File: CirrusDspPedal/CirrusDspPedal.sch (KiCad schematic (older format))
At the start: 0 parts

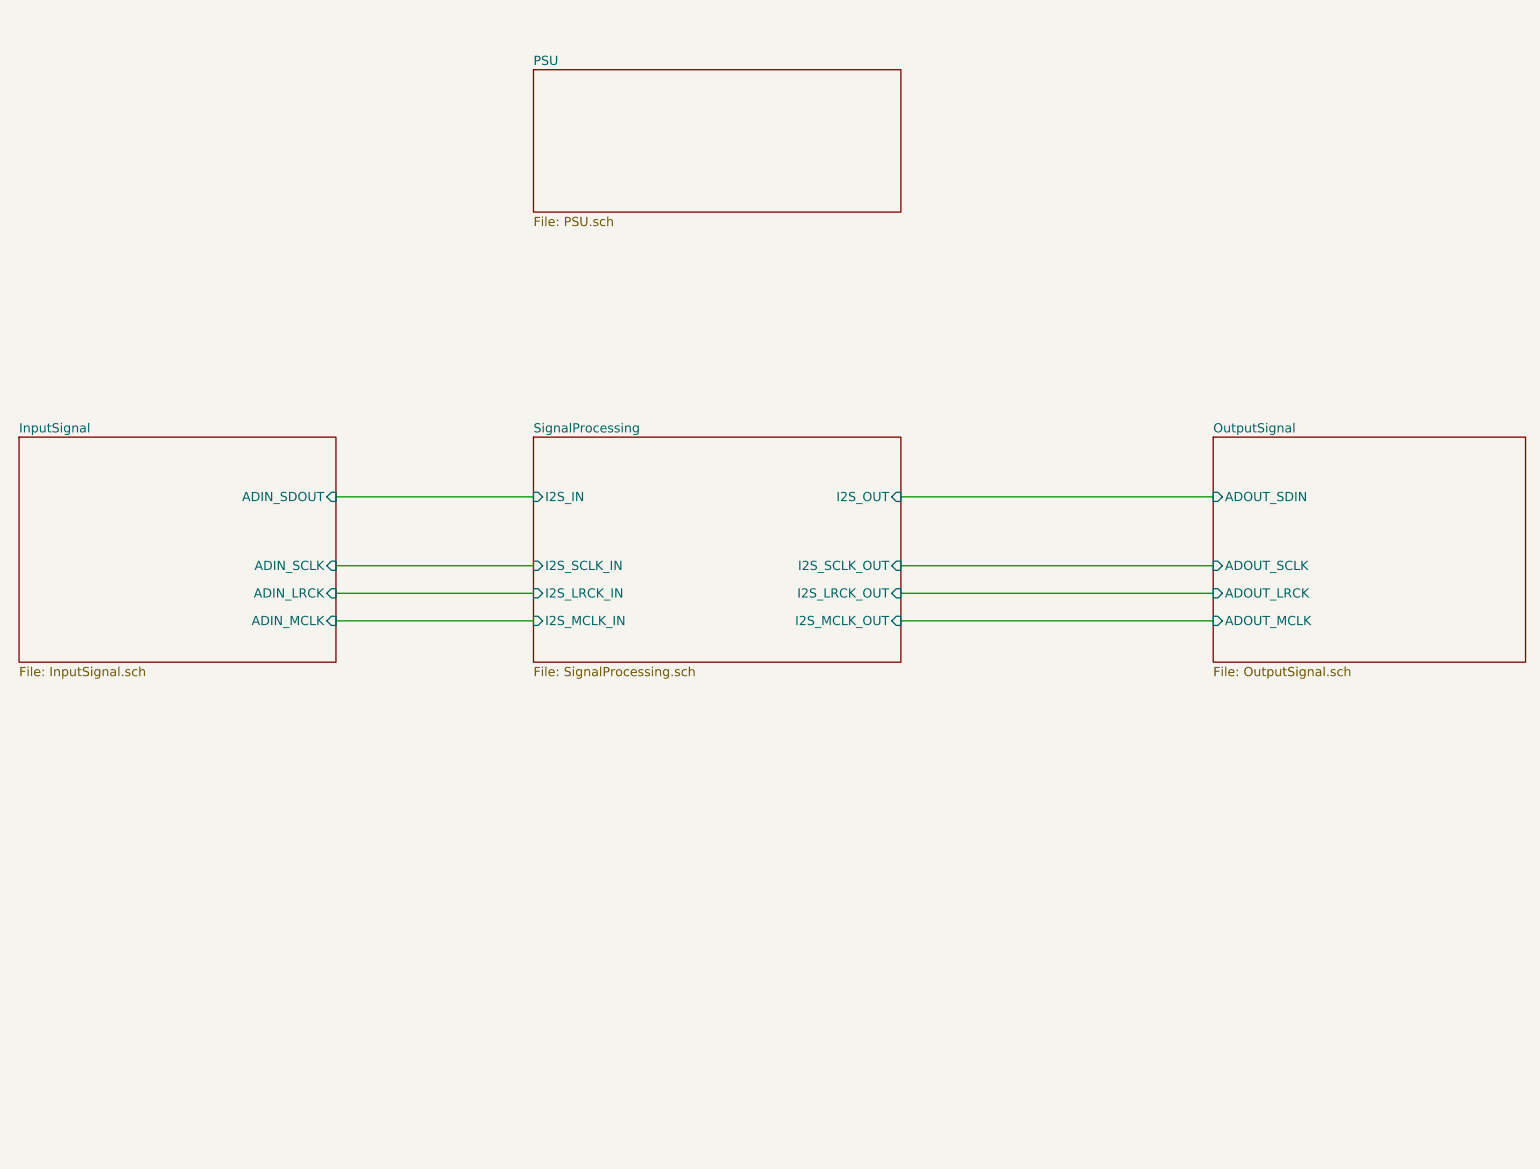
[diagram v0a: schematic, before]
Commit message: Added Footswitches and relay
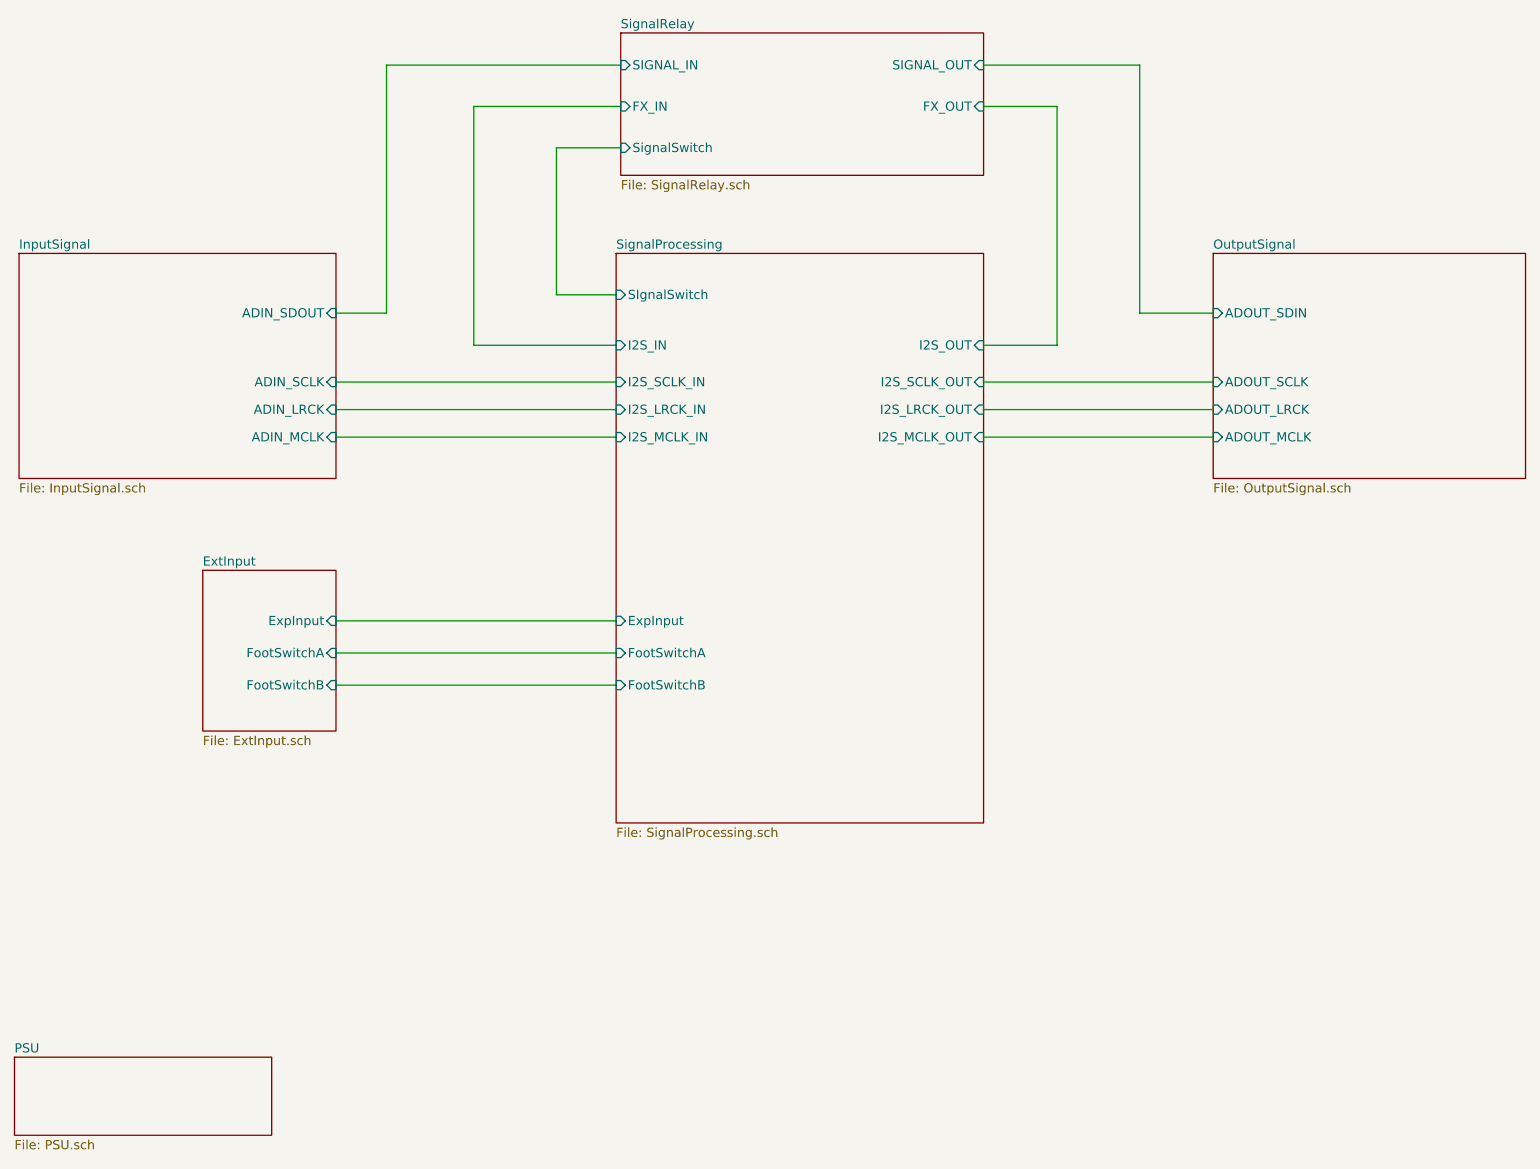
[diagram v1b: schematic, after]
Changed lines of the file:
@@
 $Descr A4 11693 8268
 encoding utf-8
-Sheet 1 8
+Sheet 1 10
 Title ""
 Date ""
@@
 $EndDescr
 $Sheet
-S 1800 3325 1725 1225
+S 1800 2325 1725 1225
 U 5F834C36
 F0 "InputSignal" 50
 F1 "InputSignal.sch" 50
-F2 "ADIN_SDOUT" I R 3525 3650 50
-F3 "ADIN_SCLK" I R 3525 4025 50
-F4 "ADIN_LRCK" I R 3525 4175 50
-F5 "ADIN_MCLK" I R 3525 4325 50
+F2 "ADIN_SDOUT" I R 3525 2650 50
+F3 "ADIN_SCLK" I R 3525 3025 50
+F4 "ADIN_LRCK" I R 3525 3175 50
+F5 "ADIN_MCLK" I R 3525 3325 50
 $EndSheet
 $Sheet
-S 8300 3325 1700 1225
+S 8300 2325 1700 1225
 U 5F834DC7
 F0 "OutputSignal" 50
 F1 "OutputSignal.sch" 50
-F2 "ADOUT_SDIN" I L 8300 3650 50
-F3 "ADOUT_SCLK" I L 8300 4025 50
-F4 "ADOUT_LRCK" I L 8300 4175 50
-F5 "ADOUT_MCLK" I L 8300 4325 50
+F2 "ADOUT_SDIN" I L 8300 2650 50
+F3 "ADOUT_SCLK" I L 8300 3025 50
+F4 "ADOUT_LRCK" I L 8300 3175 50
+F5 "ADOUT_MCLK" I L 8300 3325 50
 $EndSheet
 $Sheet
-S 4600 3325 2000 1225
+S 5050 2325 2000 3100
 U 5F834F6D
 F0 "SignalProcessing" 50
 F1 "SignalProcessing.sch" 50
-F2 "I2S_IN" I L 4600 3650 50
-F3 "I2S_OUT" I R 6600 3650 50
-F4 "I2S_MCLK_IN" I L 4600 4325 50
-F5 "I2S_SCLK_OUT" I R 6600 4025 50
-F6 "I2S_MCLK_OUT" I R 6600 4325 50
-F7 "I2S_SCLK_IN" I L 4600 4025 50
-F8 "I2S_LRCK_OUT" I R 6600 4175 50
-F9 "I2S_LRCK_IN" I L 4600 4175 50
+F2 "I2S_IN" I L 5050 2825 50
+F3 "I2S_OUT" I R 7050 2825 50
+F4 "I2S_MCLK_IN" I L 5050 3325 50
+F5 "I2S_SCLK_OUT" I R 7050 3025 50
+F6 "I2S_MCLK_OUT" I R 7050 3325 50
+F7 "I2S_SCLK_IN" I L 5050 3025 50
+F8 "I2S_LRCK_OUT" I R 7050 3175 50
+F9 "I2S_LRCK_IN" I L 5050 3175 50
+F10 "ExpInput" I L 5050 4325 50
+F11 "SIgnalSwitch" I L 5050 2550 50
+F12 "FootSwitchA" I L 5050 4500 50
+F13 "FootSwitchB" I L 5050 4675 50
 $EndSheet
 Wire Wire Line
-	3525 4325 4600 4325
+	3525 3325 5050 3325
 Wire Wire Line
-	3525 4175 4600 4175
+	3525 3175 5050 3175
 Wire Wire Line
-	3525 4025 4600 4025
+	3525 3025 5050 3025
 Wire Wire Line
-	4600 3650 3525 3650
+	7050 3025 8300 3025
 Wire Wire Line
-	6600 3650 8300 3650
+	7050 3175 8300 3175
 Wire Wire Line
-	6600 4025 8300 4025
-Wire Wire Line
-	6600 4175 8300 4175
-Wire Wire Line
-	6600 4325 8300 4325
+	7050 3325 8300 3325
 $Sheet
-S 4600 1325 2000 775
+S 1775 6700 1400 425
 U 5F95DD48
 F0 "PSU" 50
 F1 "PSU.sch" 50
 $EndSheet
+$Sheet
+S 2800 4050 725  875
+U 5F898CA5
+F0 "ExtInput" 50
+F1 "ExtInput.sch" 50
+F2 "ExpInput" I R 3525 4325 50
+F3 "FootSwitchA" I R 3525 4500 50
+F4 "FootSwitchB" I R 3525 4675 50
+$EndSheet
+Wire Wire Line
+	3525 4325 5050 4325
+$Sheet
+S 5075 1125 1975 775
+U 5F8531C2
+F0 "SignalRelay" 50
+F1 "SignalRelay.sch" 50
+F2 "SignalSwitch" I L 5075 1750 50
+F3 "SIGNAL_IN" I L 5075 1300 50
+F4 "SIGNAL_OUT" I R 7050 1300 50
+F5 "FX_IN" I L 5075 1525 50
+F6 "FX_OUT" I R 7050 1525 50
+$EndSheet
+Wire Wire Line
+	3525 2650 3800 2650
+Wire Wire Line
+	3800 2650 3800 1300
+Wire Wire Line
+	3800 1300 5075 1300
+Wire Wire Line
+	7050 1300 7900 1300
+Wire Wire Line
+	7900 1300 7900 2650
+Wire Wire Line
+	7900 2650 8300 2650
+Wire Wire Line
+	7050 1525 7450 1525
+Wire Wire Line
+	7450 1525 7450 2825
+Wire Wire Line
+	7450 2825 7050 2825
+Wire Wire Line
+	5050 2825 4275 2825
+Wire Wire Line
+	4275 2825 4275 1525
+Wire Wire Line
+	4275 1525 5075 1525
+Wire Wire Line
+	5050 2550 4725 2550
+Wire Wire Line
+	4725 2550 4725 1750
+Wire Wire Line
+	4725 1750 5075 1750
+Wire Wire Line
+	5050 4500 3525 4500
+Wire Wire Line
+	3525 4675 5050 4675
 $EndSCHEMATC

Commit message: updates
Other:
- note added: "AnalogInput"
- note added: "DigitalInput"
- note added: "DigitalOutput"
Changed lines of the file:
@@
 F0 "SignalProcessing" 50
 F1 "SignalProcessing.sch" 50
-F2 "I2S_IN" I L 5050 2825 50
-F3 "I2S_OUT" I R 7050 2825 50
+F2 "I2S_IN" I L 5050 2875 50
+F3 "I2S_OUT" I R 7050 2875 50
 F4 "I2S_MCLK_IN" I L 5050 3325 50
 F5 "I2S_SCLK_OUT" I R 7050 3025 50
@@
 	7900 2650 8300 2650
 Wire Wire Line
-	7050 1525 7450 1525
+	7050 1525 7625 1525
 Wire Wire Line
-	7450 1525 7450 2825
+	7625 1525 7625 2875
 Wire Wire Line
-	7450 2825 7050 2825
+	7625 2875 7050 2875
 Wire Wire Line
-	5050 2825 4275 2825
+	5050 2875 4100 2875
 Wire Wire Line
-	4275 2825 4275 1525
+	4100 2875 4100 1525
 Wire Wire Line
-	4275 1525 5075 1525
+	4100 1525 5075 1525
 Wire Wire Line
-	5050 2550 4725 2550
+	5050 2550 4450 2550
 Wire Wire Line
-	4725 2550 4725 1750
+	4450 2550 4450 1750
 Wire Wire Line
-	4725 1750 5075 1750
+	4450 1750 5075 1750
 Wire Wire Line
 	5050 4500 3525 4500
 Wire Wire Line
 	3525 4675 5050 4675
+Text Notes 4000 4325 0    50   ~ 0
+AnalogInput
+Text Notes 4000 4500 0    50   ~ 0
+DigitalInput
+Text Notes 4000 4675 0    50   ~ 0
+DigitalInput
+Text Notes 4500 2550 0    50   ~ 0
+DigitalOutput
 $EndSCHEMATC

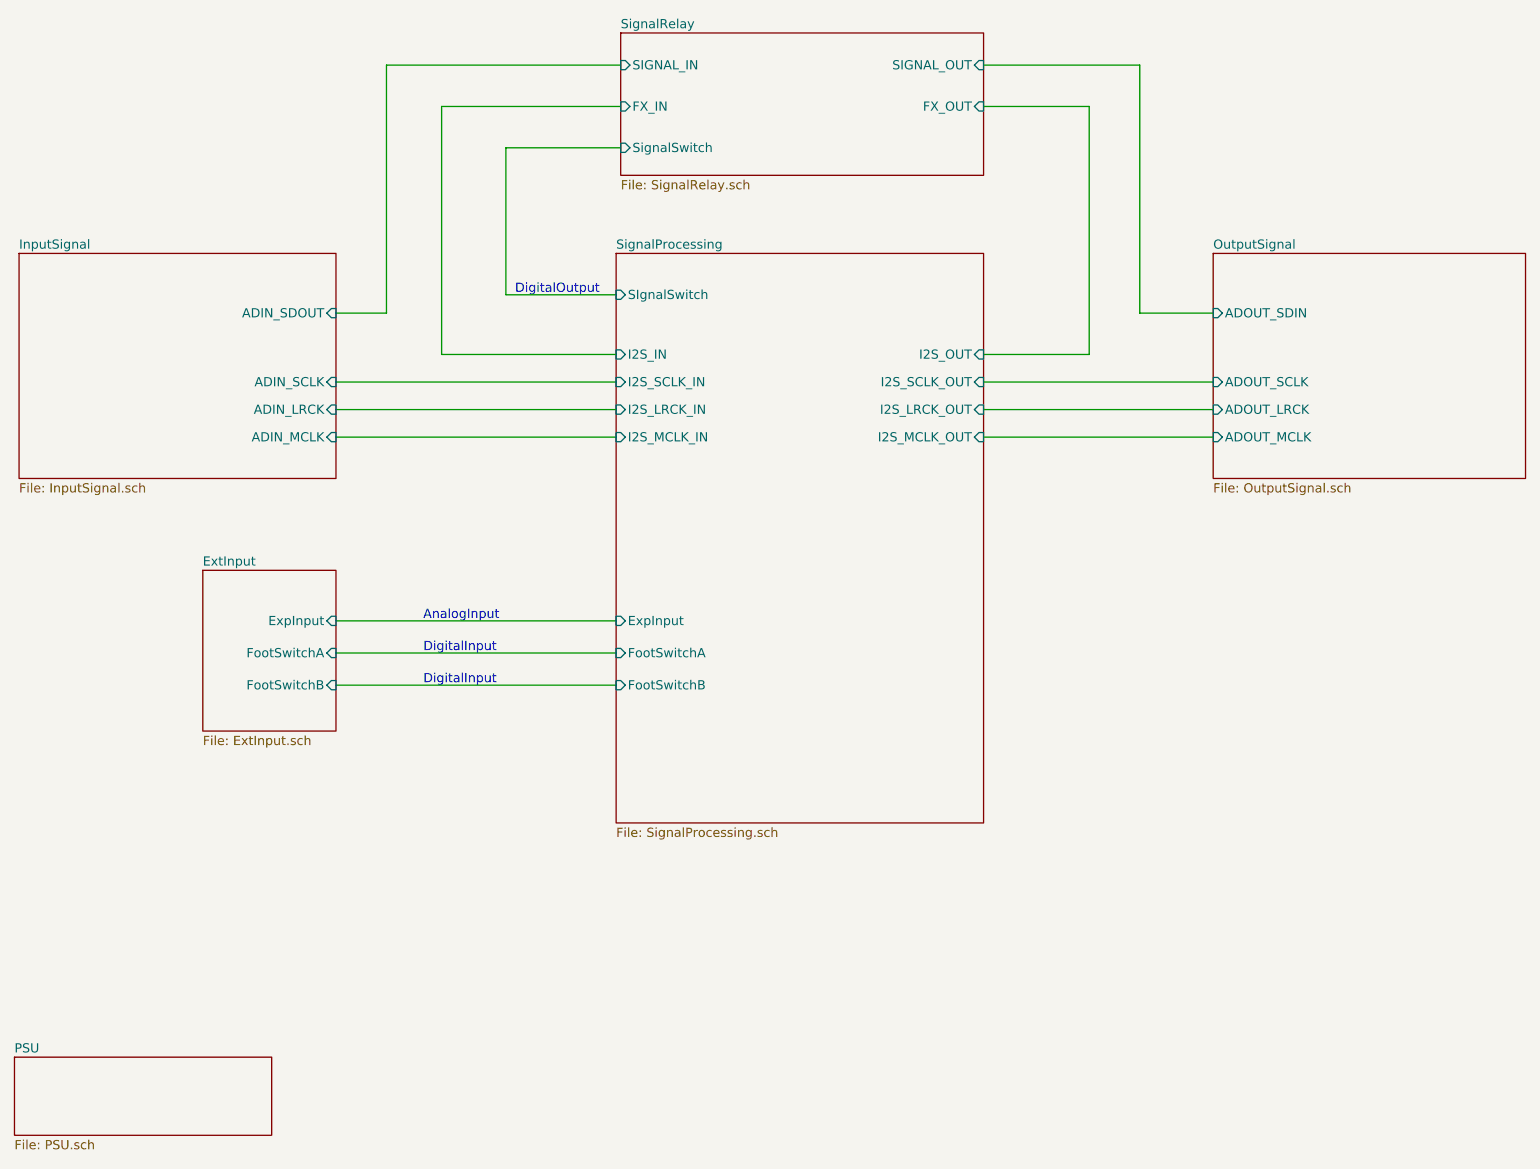
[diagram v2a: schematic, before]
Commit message: Added UserPots and RGB LEDS
Updated schema docs
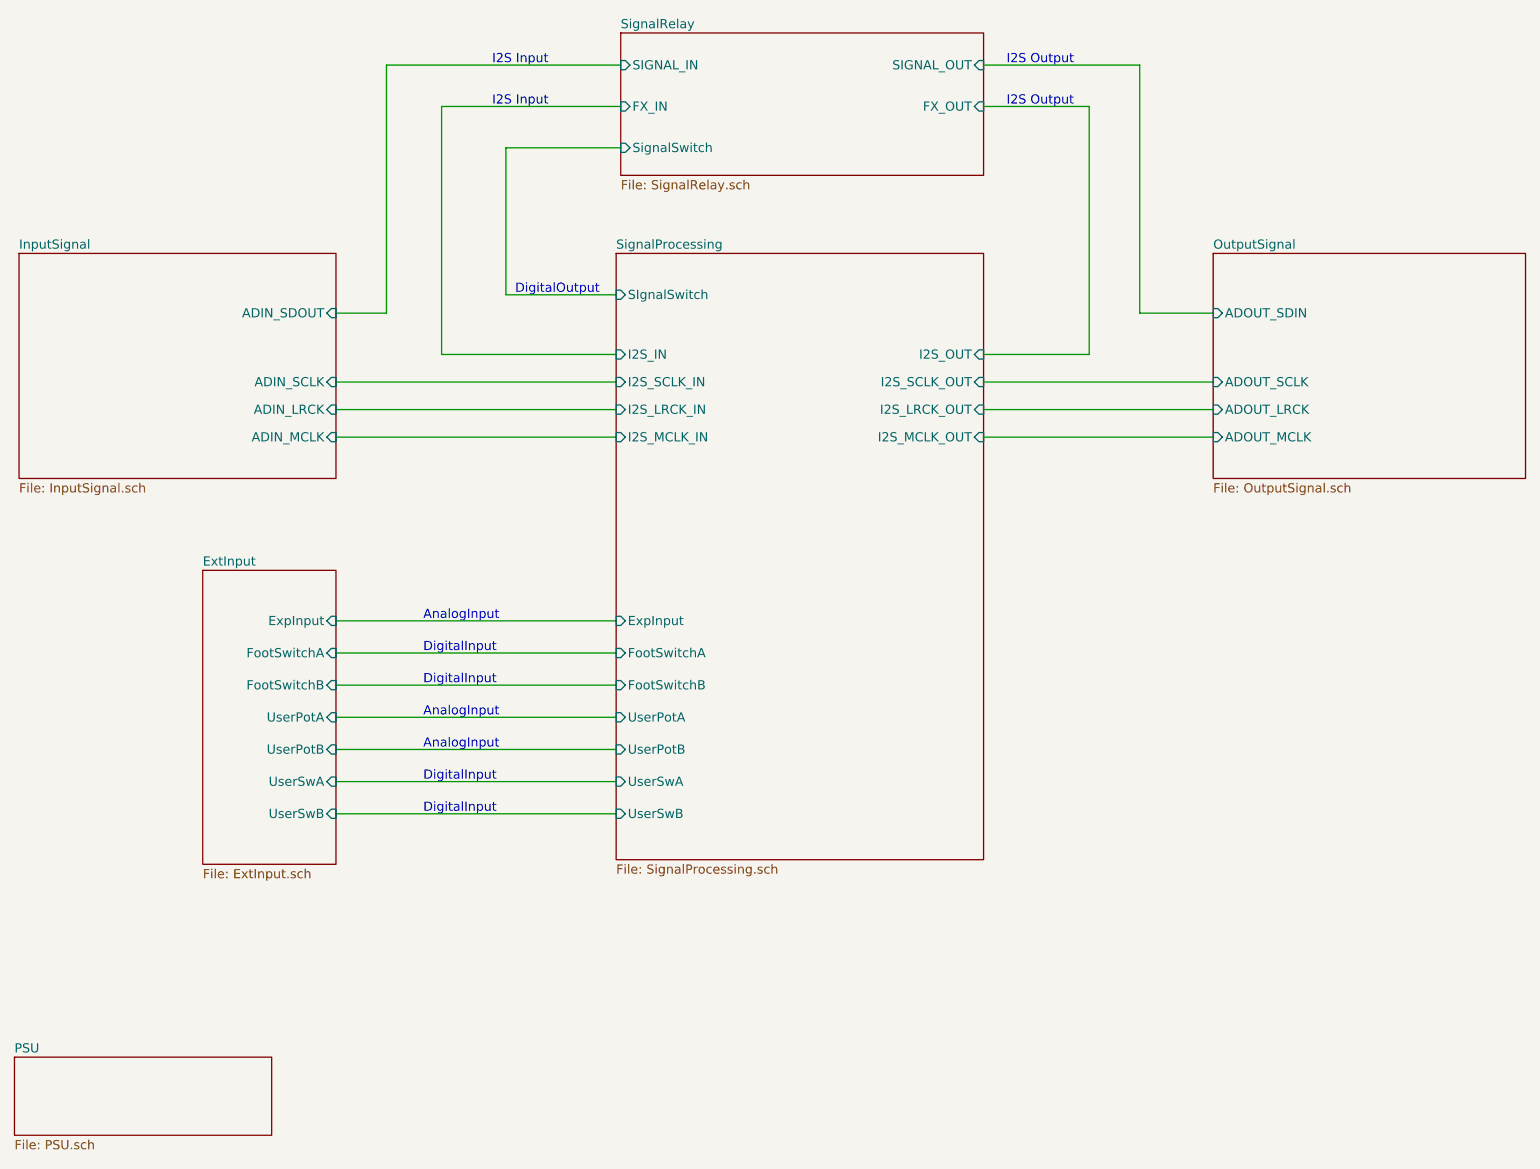
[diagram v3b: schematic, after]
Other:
- note added: "I2S Input"
- note added: "I2S Output"
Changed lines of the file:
@@
 F5 "ADOUT_MCLK" I L 8300 3325 50
-$EndSheet
-$Sheet
-S 5050 2325 2000 3100
-U 5F834F6D
-F0 "SignalProcessing" 50
-F1 "SignalProcessing.sch" 50
-F2 "I2S_IN" I L 5050 2875 50
-F3 "I2S_OUT" I R 7050 2875 50
-F4 "I2S_MCLK_IN" I L 5050 3325 50
-F5 "I2S_SCLK_OUT" I R 7050 3025 50
-F6 "I2S_MCLK_OUT" I R 7050 3325 50
-F7 "I2S_SCLK_IN" I L 5050 3025 50
-F8 "I2S_LRCK_OUT" I R 7050 3175 50
-F9 "I2S_LRCK_IN" I L 5050 3175 50
-F10 "ExpInput" I L 5050 4325 50
-F11 "SIgnalSwitch" I L 5050 2550 50
-F12 "FootSwitchA" I L 5050 4500 50
-F13 "FootSwitchB" I L 5050 4675 50
 $EndSheet
 Wire Wire Line
@@
 F0 "PSU" 50
 F1 "PSU.sch" 50
-$EndSheet
-$Sheet
-S 2800 4050 725  875
-U 5F898CA5
-F0 "ExtInput" 50
-F1 "ExtInput.sch" 50
-F2 "ExpInput" I R 3525 4325 50
-F3 "FootSwitchA" I R 3525 4500 50
-F4 "FootSwitchB" I R 3525 4675 50
 $EndSheet
 Wire Wire Line
@@
 Text Notes 4500 2550 0    50   ~ 0
 DigitalOutput
+Wire Wire Line
+	3525 4850 5050 4850
+Wire Wire Line
+	3525 5025 5050 5025
+Text Notes 4000 4850 0    50   ~ 0
+AnalogInput
+Text Notes 4000 5025 0    50   ~ 0
+AnalogInput
+Text Notes 4375 1300 0    50   ~ 0
+I2S Input
+Text Notes 4375 1525 0    50   ~ 0
+I2S Input
+Text Notes 7175 1300 0    50   ~ 0
+I2S Output
+Text Notes 7175 1525 0    50   ~ 0
+I2S Output
+Wire Wire Line
+	3525 5200 5050 5200
+Wire Wire Line
+	3525 5375 5050 5375
+Text Notes 4000 5200 0    50   ~ 0
+DigitalInput
+Text Notes 4000 5375 0    50   ~ 0
+DigitalInput
+$Sheet
+S 5050 2325 2000 3300
+U 5F834F6D
+F0 "SignalProcessing" 50
+F1 "SignalProcessing.sch" 50
+F2 "I2S_IN" I L 5050 2875 50
+F3 "I2S_OUT" I R 7050 2875 50
+F4 "I2S_MCLK_IN" I L 5050 3325 50
+F5 "I2S_SCLK_OUT" I R 7050 3025 50
+F6 "I2S_MCLK_OUT" I R 7050 3325 50
+F7 "I2S_SCLK_IN" I L 5050 3025 50
+F8 "I2S_LRCK_OUT" I R 7050 3175 50
+F9 "I2S_LRCK_IN" I L 5050 3175 50
+F10 "ExpInput" I L 5050 4325 50
+F11 "SIgnalSwitch" I L 5050 2550 50
+F12 "FootSwitchA" I L 5050 4500 50
+F13 "FootSwitchB" I L 5050 4675 50
+F14 "UserPotA" I L 5050 4850 50
+F15 "UserPotB" I L 5050 5025 50
+F16 "UserSwA" I L 5050 5200 50
+F17 "UserSwB" I L 5050 5375 50
+$EndSheet
+$Sheet
+S 2800 4050 725  1600
+U 5F898CA5
+F0 "ExtInput" 50
+F1 "ExtInput.sch" 50
+F2 "ExpInput" I R 3525 4325 50
+F3 "FootSwitchA" I R 3525 4500 50
+F4 "FootSwitchB" I R 3525 4675 50
+F5 "UserPotA" I R 3525 4850 50
+F6 "UserPotB" I R 3525 5025 50
+F7 "UserSwA" I R 3525 5200 50
+F8 "UserSwB" I R 3525 5375 50
+$EndSheet
 $EndSCHEMATC
